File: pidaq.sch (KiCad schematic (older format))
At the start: 41 parts, among them J1 Screw_Terminal_01x08, J2 Screw_Terminal_01x08, J3 Screw_Terminal_01x10, J4 Screw_Terminal_01x10, J5 Conn_01x02_Male, J6 Conn_01x08_Female, U1 LTC2984CLX-DNP, U2 LTC2418IGN-DNP

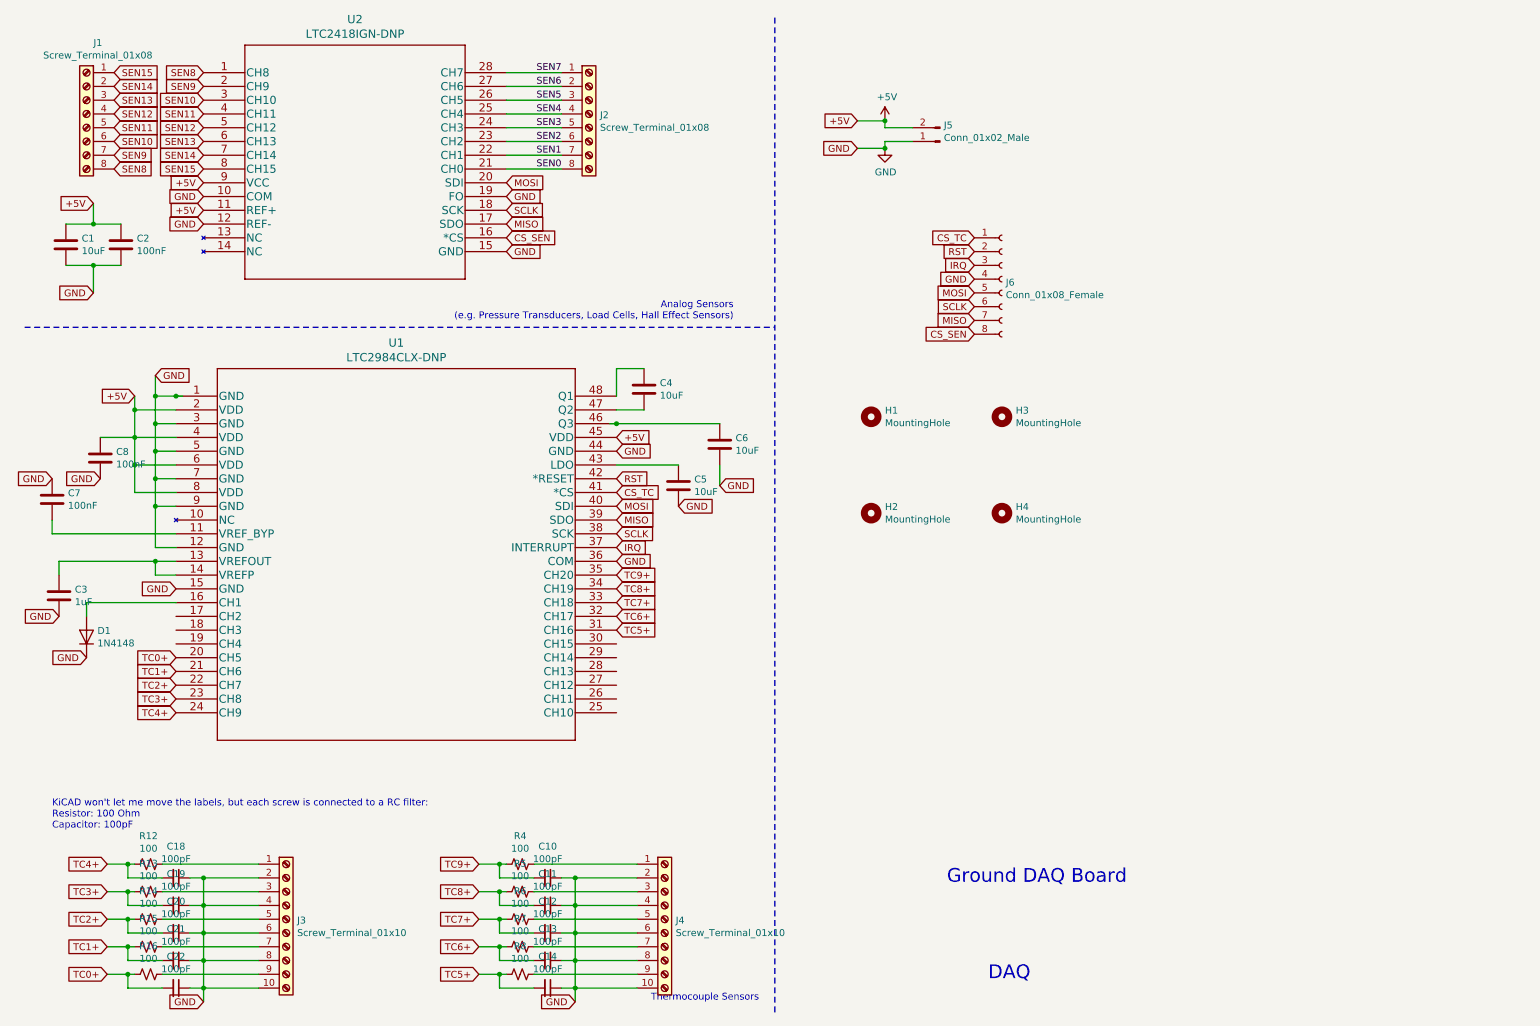
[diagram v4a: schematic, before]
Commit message: add level shifters to MISO
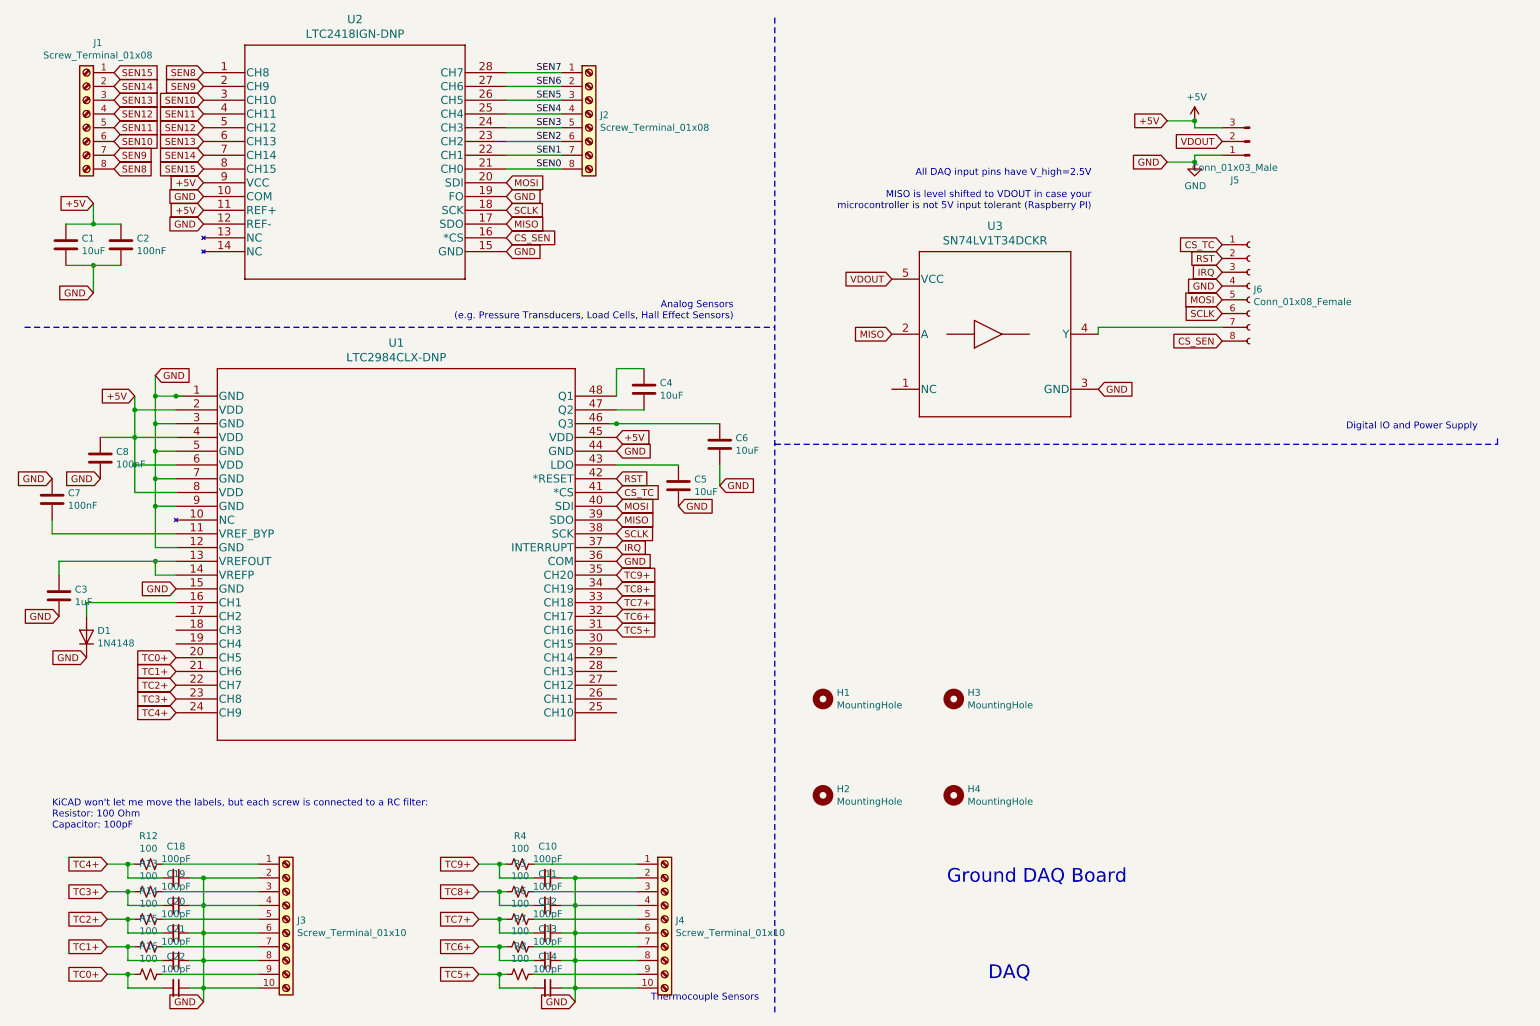
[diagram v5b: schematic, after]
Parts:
- removed J5: Conn_01x02_Male, Connector_PinHeader_2.54mm:PinHeader_1x02_P2.54mm_Vertical, symbol Connector:Conn_01x02_Male
- added J5: Conn_01x03_Male, Connector_PinHeader_2.54mm:PinHeader_1x03_P2.54mm_Vertical, symbol Connector:Conn_01x03_Male
- added U3: SN74LV1T34DCKR, proj_footprints:SN74LV1T34DCKR, symbol SN74LV1T34:SN74LV1T34DCKR
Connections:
- net +5V: now also J5.3 (Pin_3)
- net GND: now also J5.1 (Pin_1), U3.3 (GND)
- net MISO: now also U3.2 (A); no longer J6.7 (Pin_7)
- new net: J6.7 (Pin_7), U3.4 (Y)
- new net VDOUT: J5.2 (Pin_2), U3.5 (VCC)
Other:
- note added: "All DAQ input pins have V_high=2.5V\n\nMISO is level shifted to VDOUT in case your\nmicrocontroller is not 5V input tolerant (Raspberry PI)"
- note added: "Digital IO and Power Supply"
- moved on the sheet: H1, H2, H3, H4, J6
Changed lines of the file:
@@
 L power:+5V #PWR0101
 U 1 1 5F02F8BC
-P 6700 1300
-F 0 "#PWR0101" H 6700 1150 50  0001 C CNN
-F 1 "+5V" H 6715 1473 50  0000 C CNN
-F 2 "" H 6700 1300 50  0001 C CNN
-F 3 "" H 6700 1300 50  0001 C CNN
-	1    6700 1300
-	1    0    0    -1
-$EndComp
-Text GLabel 6500 1300 0    50   Input ~ 0
+P 8950 1300
+F 0 "#PWR0101" H 8950 1150 50  0001 C CNN
+F 1 "+5V" H 8965 1473 50  0000 C CNN
+F 2 "" H 8950 1300 50  0001 C CNN
+F 3 "" H 8950 1300 50  0001 C CNN
+	1    8950 1300
+	1    0    0    -1
+$EndComp
+Text GLabel 8750 1300 0    50   Input ~ 0
 +5V
-Text GLabel 6500 1500 0    50   Input ~ 0
+Text GLabel 8750 1600 0    50   Input ~ 0
 GND
 $Comp
 L power:GND #PWR0102
 U 1 1 5F02FCDF
-P 6700 1500
-F 0 "#PWR0102" H 6700 1250 50  0001 C CNN
-F 1 "GND" H 6705 1327 50  0000 C CNN
-F 2 "" H 6700 1500 50  0001 C CNN
-F 3 "" H 6700 1500 50  0001 C CNN
-	1    6700 1500
-	1    0    0    -1
-$EndComp
-Wire Wire Line
-	6700 1300 6500 1300
-Wire Wire Line
-	6500 1500 6700 1500
-$Comp
-L Connector:Conn_01x02_Male J5
-U 1 1 5F061D74
-P 7100 1450
-F 0 "J5" H 7072 1332 50  0000 R CNN
-F 1 "Conn_01x02_Male" H 7072 1423 50  0000 R CNN
-F 2 "Connector_PinHeader_2.54mm:PinHeader_1x02_P2.54mm_Vertical" H 7100 1450 50  0001 C CNN
-F 3 "~" H 7100 1450 50  0001 C CNN
-	1    7100 1450
-	-1   0    0    1
-$EndComp
-Wire Wire Line
-	6900 1350 6700 1350
-Wire Wire Line
-	6700 1350 6700 1300
-Connection ~ 6700 1300
-Wire Wire Line
-	6900 1450 6700 1450
-Wire Wire Line
-	6700 1450 6700 1500
-Connection ~ 6700 1500
+P 8950 1600
+F 0 "#PWR0102" H 8950 1350 50  0001 C CNN
+F 1 "GND" H 8955 1427 50  0000 C CNN
+F 2 "" H 8950 1600 50  0001 C CNN
+F 3 "" H 8950 1600 50  0001 C CNN
+	1    8950 1600
+	1    0    0    -1
+$EndComp
+Wire Wire Line
+	8950 1300 8750 1300
+Wire Wire Line
+	8750 1600 8950 1600
+Wire Wire Line
+	9150 1350 8950 1350
+Wire Wire Line
+	8950 1350 8950 1300
+Connection ~ 8950 1300
+Wire Wire Line
+	9150 1550 8950 1550
+Wire Wire Line
+	8950 1550 8950 1600
+Connection ~ 8950 1600
 $Comp
 L Connector:Conn_01x08_Female J6
 U 1 1 5F088E4C
-P 7550 2450
-F 0 "J6" H 7578 2426 50  0000 L CNN
-F 1 "Conn_01x08_Female" H 7578 2335 50  0000 L CNN
-F 2 "Connector_PinHeader_2.54mm:PinHeader_1x08_P2.54mm_Vertical" H 7550 2450 50  0001 C CNN
-F 3 "~" H 7550 2450 50  0001 C CNN
-	1    7550 2450
-	1    0    0    -1
-$EndComp
-Text GLabel 7350 2850 0    50   Input ~ 0
+P 9350 2500
+F 0 "J6" H 9378 2476 50  0000 L CNN
+F 1 "Conn_01x08_Female" H 9378 2385 50  0000 L CNN
+F 2 "Connector_PinHeader_2.54mm:PinHeader_1x08_P2.54mm_Vertical" H 9350 2500 50  0001 C CNN
+F 3 "~" H 9350 2500 50  0001 C CNN
+	1    9350 2500
+	1    0    0    -1
+$EndComp
+Text GLabel 9150 2900 0    50   Input ~ 0
 CS_SEN
-Text GLabel 7350 2150 0    50   Input ~ 0
+Text GLabel 9150 2200 0    50   Input ~ 0
 CS_TC
-Text GLabel 7350 2250 0    50   Input ~ 0
+Text GLabel 9150 2300 0    50   Input ~ 0
 RST
-Text GLabel 7350 2350 0    50   Input ~ 0
+Text GLabel 9150 2400 0    50   Input ~ 0
 IRQ
-Text GLabel 7350 2450 0    50   Input ~ 0
-GND
-Text GLabel 7350 2650 0    50   Input ~ 0
+Text GLabel 9150 2500 0    50   Input ~ 0
+GND
+Text GLabel 9150 2700 0    50   Input ~ 0
 SCLK
-Text GLabel 7350 2550 0    50   Input ~ 0
+Text GLabel 9150 2600 0    50   Input ~ 0
 MOSI
-Text GLabel 7350 2750 0    50   Input ~ 0
+Text GLabel 6750 2850 0    50   Input ~ 0
 MISO
 $Comp
@@
 L Mechanical:MountingHole H1
 U 1 1 5ED3CDC2
-P 6600 3450
-F 0 "H1" H 6700 3496 50  0000 L CNN
-F 1 "MountingHole" H 6700 3405 50  0000 L CNN
-F 2 "MountingHole:MountingHole_3.2mm_M3" H 6600 3450 50  0001 C CNN
-F 3 "~" H 6600 3450 50  0001 C CNN
-	1    6600 3450
+P 6250 5500
+F 0 "H1" H 6350 5546 50  0000 L CNN
+F 1 "MountingHole" H 6350 5455 50  0000 L CNN
+F 2 "MountingHole:MountingHole_3.2mm_M3" H 6250 5500 50  0001 C CNN
+F 3 "~" H 6250 5500 50  0001 C CNN
+	1    6250 5500
 	1    0    0    -1
 $EndComp
@@
 L Mechanical:MountingHole H3
 U 1 1 5ED3DEFD
-P 7550 3450
-F 0 "H3" H 7650 3496 50  0000 L CNN
-F 1 "MountingHole" H 7650 3405 50  0000 L CNN
-F 2 "MountingHole:MountingHole_3.2mm_M3" H 7550 3450 50  0001 C CNN
-F 3 "~" H 7550 3450 50  0001 C CNN
-	1    7550 3450
+P 7200 5500
+F 0 "H3" H 7300 5546 50  0000 L CNN
+F 1 "MountingHole" H 7300 5455 50  0000 L CNN
+F 2 "MountingHole:MountingHole_3.2mm_M3" H 7200 5500 50  0001 C CNN
+F 3 "~" H 7200 5500 50  0001 C CNN
+	1    7200 5500
 	1    0    0    -1
 $EndComp
@@
 L Mechanical:MountingHole H2
 U 1 1 5ED3EC92
-P 6600 4150
-F 0 "H2" H 6700 4196 50  0000 L CNN
-F 1 "MountingHole" H 6700 4105 50  0000 L CNN
-F 2 "MountingHole:MountingHole_3.2mm_M3" H 6600 4150 50  0001 C CNN
-F 3 "~" H 6600 4150 50  0001 C CNN
-	1    6600 4150
+P 6250 6200
+F 0 "H2" H 6350 6246 50  0000 L CNN
+F 1 "MountingHole" H 6350 6155 50  0000 L CNN
+F 2 "MountingHole:MountingHole_3.2mm_M3" H 6250 6200 50  0001 C CNN
+F 3 "~" H 6250 6200 50  0001 C CNN
+	1    6250 6200
 	1    0    0    -1
 $EndComp
@@
 L Mechanical:MountingHole H4
 U 1 1 5ED3F653
-P 7550 4150
-F 0 "H4" H 7650 4196 50  0000 L CNN
-F 1 "MountingHole" H 7650 4105 50  0000 L CNN
-F 2 "MountingHole:MountingHole_3.2mm_M3" H 7550 4150 50  0001 C CNN
-F 3 "~" H 7550 4150 50  0001 C CNN
-	1    7550 4150
+P 7200 6200
+F 0 "H4" H 7300 6246 50  0000 L CNN
+F 1 "MountingHole" H 7300 6155 50  0000 L CNN
+F 2 "MountingHole:MountingHole_3.2mm_M3" H 7200 6200 50  0001 C CNN
+F 3 "~" H 7200 6200 50  0001 C CNN
+	1    7200 6200
 	1    0    0    -1
 $EndComp
@@
 Text Notes 7450 7550 0    100  ~ 0
 DAQ
+$Comp
+L SN74LV1T34:SN74LV1T34DCKR U3
+U 1 1 5ED7754A
+P 7450 2850
+F 0 "U3" H 7500 3636 60  0000 C CNN
+F 1 "SN74LV1T34DCKR" H 7500 3530 60  0000 C CNN
+F 2 "proj_footprints:SN74LV1T34DCKR" H 7450 2790 60  0001 C CNN
+F 3 "" H 7450 2850 60  0000 C CNN
+	1    7450 2850
+	1    0    0    -1
+$EndComp
+$Comp
+L Connector:Conn_01x03_Male J5
+U 1 1 5EDA59D3
+P 9350 1450
+F 0 "J5" H 9458 1731 50  0000 C CNN
+F 1 "Conn_01x03_Male" H 9458 1640 50  0000 C CNN
+F 2 "Connector_PinHeader_2.54mm:PinHeader_1x03_P2.54mm_Vertical" H 9350 1450 50  0001 C CNN
+F 3 "~" H 9350 1450 50  0001 C CNN
+	1    9350 1450
+	-1   0    0    1
+$EndComp
+Text GLabel 9150 1450 0    50   Input ~ 0
+VDOUT
+Text GLabel 6750 2450 0    50   Input ~ 0
+VDOUT
+Text GLabel 8250 3250 2    50   Input ~ 0
+GND
+Wire Wire Line
+	9150 2800 8250 2800
+Wire Wire Line
+	8250 2800 8250 2850
+Wire Notes Line
+	5900 3650 11150 3650
+Wire Notes Line
+	11150 3650 11150 3600
+Text Notes 10050 3550 0    50   ~ 0
+Digital IO and Power Supply
+Text Notes 8200 1950 2    50   ~ 0
+All DAQ input pins have V_high=2.5V\n\nMISO is level shifted to VDOUT in case your\nmicrocontroller is not 5V input tolerant (Raspberry PI)
 $EndSCHEMATC
